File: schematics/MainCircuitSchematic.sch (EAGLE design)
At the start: 13 parts

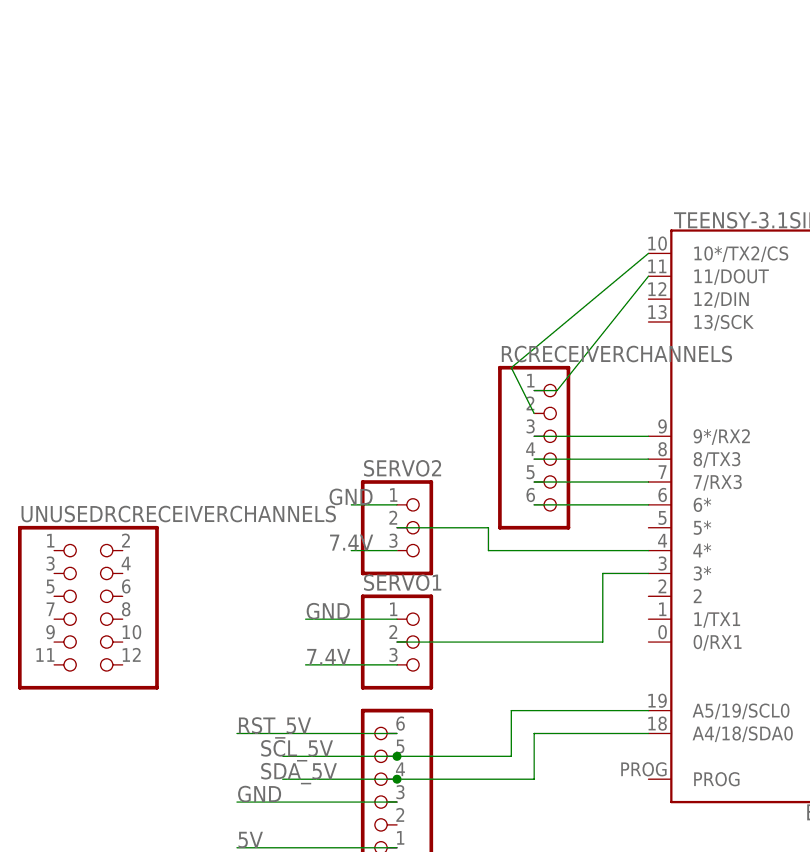
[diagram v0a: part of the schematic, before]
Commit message: Add files via upload
fixed receiver and servo pins
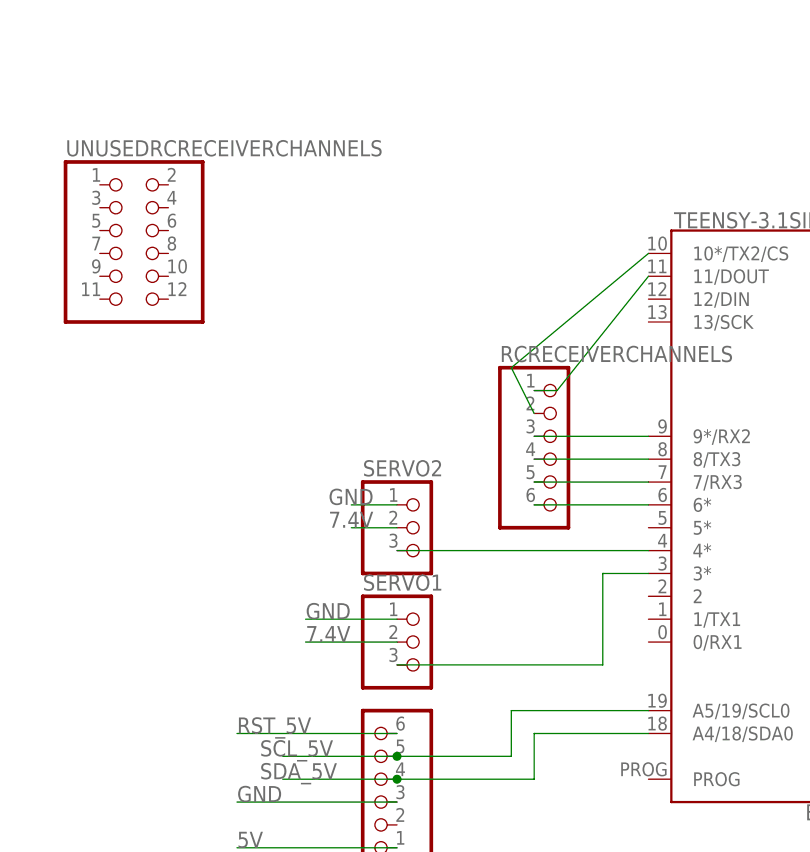
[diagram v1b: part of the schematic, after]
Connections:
- net 7.4V: now also SERVO1.2, SERVO2.2; no longer SERVO1.3, SERVO2.3
- net N$7: now also SERVO2.3; no longer SERVO2.2
- net N$8: now also SERVO1.3; no longer SERVO1.2
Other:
- moved on the sheet: UNUSEDRCRECEIVERCHANNELS
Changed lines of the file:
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@@
 <attribute name="VALUE" x="113.03" y="71.12" size="1.778" layer="96"/>
 </instance>
-<instance part="UNUSEDRCRECEIVERCHANNELS" gate="A" x="0" y="53.34" smashed="yes">
-<attribute name="NAME" x="-6.35" y="61.595" size="1.778" layer="95"/>
+<instance part="UNUSEDRCRECEIVERCHANNELS" gate="A" x="5.08" y="93.98" smashed="yes">
+<attribute name="NAME" x="-1.27" y="102.235" size="1.778" layer="95"/>
 </instance>
 <instance part="RECIEVGND" gate="G$1" x="106.68" y="111.76" smashed="yes">
@@
 </segment>
 <segment>
-<pinref part="SERVO2" gate="A" pin="3"/>
-<wire x1="35.56" y1="58.42" x2="30.48" y2="58.42" width="0.1524" layer="91"/>
-<label x="27.94" y="58.42" size="1.778" layer="95"/>
+<pinref part="SERVO2" gate="A" pin="2"/>
+<wire x1="35.56" y1="60.96" x2="30.48" y2="60.96" width="0.1524" layer="91"/>
+<label x="27.94" y="60.96" size="1.778" layer="95"/>
 </segment>
 <segment>
-<pinref part="SERVO1" gate="A" pin="3"/>
-<wire x1="35.56" y1="45.72" x2="25.4" y2="45.72" width="0.1524" layer="91"/>
-<label x="25.4" y="45.72" size="1.778" layer="95"/>
+<pinref part="SERVO1" gate="A" pin="2"/>
+<wire x1="35.56" y1="48.26" x2="25.4" y2="48.26" width="0.1524" layer="91"/>
+<label x="25.4" y="48.26" size="1.778" layer="95"/>
 </segment>
 </net>
@@
 <net name="N$7" class="0">
 <segment>
-<pinref part="SERVO2" gate="A" pin="2"/>
-<wire x1="35.56" y1="60.96" x2="45.72" y2="60.96" width="0.1524" layer="91"/>
-<wire x1="45.72" y1="60.96" x2="45.72" y2="58.42" width="0.1524" layer="91"/>
+<pinref part="SERVO2" gate="A" pin="3"/>
 <pinref part="B1" gate="G$1" pin="4*"/>
-<wire x1="45.72" y1="58.42" x2="63.5" y2="58.42" width="0.1524" layer="91"/>
+<wire x1="35.56" y1="58.42" x2="63.5" y2="58.42" width="0.1524" layer="91"/>
 </segment>
 </net>
 <net name="N$8" class="0">
 <segment>
-<pinref part="SERVO1" gate="A" pin="2"/>
-<wire x1="35.56" y1="48.26" x2="58.42" y2="48.26" width="0.1524" layer="91"/>
-<wire x1="58.42" y1="48.26" x2="58.42" y2="55.88" width="0.1524" layer="91"/>
+<pinref part="SERVO1" gate="A" pin="3"/>
+<wire x1="35.56" y1="45.72" x2="58.42" y2="45.72" width="0.1524" layer="91"/>
+<wire x1="58.42" y1="45.72" x2="58.42" y2="55.88" width="0.1524" layer="91"/>
 <pinref part="B1" gate="G$1" pin="3*"/>
 <wire x1="58.42" y1="55.88" x2="63.5" y2="55.88" width="0.1524" layer="91"/>
